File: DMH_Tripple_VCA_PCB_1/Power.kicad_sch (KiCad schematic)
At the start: 14 parts, among them J0 Conn_01x01, J100 IDC_02x05, J101 IDC_02x08

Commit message: Schematic in progress
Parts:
- removed C5: 47uF, Capacitor_THT:CP_Radial_D4.0mm_P1.50mm, symbol Device:C_Polarized
- removed C6: 100nF, Capacitor_THT:C_Disc_D4.3mm_W1.9mm_P5.00mm, symbol Device:C
- removed D3, D5: SB140+, Diode_THT:D_DO-41_SOD81_P10.16mm_Horizontal, symbol SynthStuff:Power_Bus_Schotty_+
- removed D4: SB140-, Diode_THT:D_DO-41_SOD81_P10.16mm_Horizontal, symbol SynthStuff:Power_Bus_Schotty_-
- removed J101: IDC_02x08, SynthStuff:IDC-Header_2x08_P2.54mm_Vertical_Eurorack, symbol SynthStuff:Eurorack_Power_Connector_16Pin
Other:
- note removed: "Delete what's not needed!"

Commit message: Finished Schematic
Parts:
- added C5, C6, C7, C8: 100nF, Capacitor_THT:C_Disc_D4.3mm_W1.9mm_P5.00mm, symbol Device:C
- added U1, U2: TL074, symbol Amplifier_Operational:TL074
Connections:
- net +12V: now also C5.1, C7.1, U1.4 (V+), U2.4 (V+)
- net -12V: now also C6.2, C8.2, U1.11 (V-), U2.11 (V-)
- net GND: now also C5.2, C6.1, C7.2, C8.1

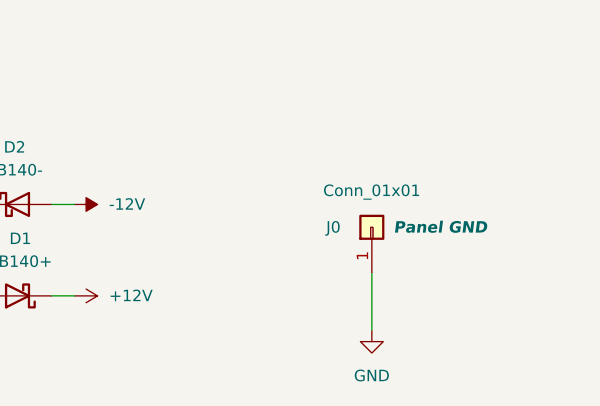
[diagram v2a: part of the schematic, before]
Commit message: PCB 1 component positioning in progress
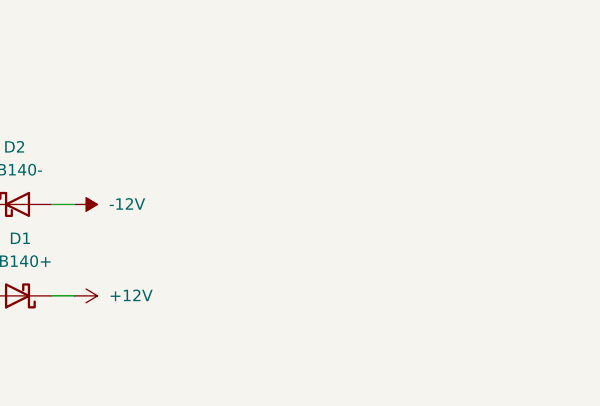
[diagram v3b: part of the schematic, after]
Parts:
- removed J0: Conn_01x01, Connector_PinHeader_2.54mm:PinHeader_1x01_P2.54mm_Vertical, symbol Connector_Generic:Conn_01x01
- U1, U2: footprint (none) -> Package_DIP:DIP-14_W7.62mm_Socket
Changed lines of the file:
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@@
-	(wire
-		(pts
-			(xy 152.4 182.88) (xy 152.4 189.23)
-		)
-		(stroke
-			(width 0)
-			(type default)
-		)
-	)
 	(wire
 		(pts
@@
 			)
 		)
-		(property "Footprint" ""
+		(property "Footprint" "Package_DIP:DIP-14_W7.62mm_Socket"
 			(at 52.07 118.11 0)
 			(effects
@@
 				)
 				(hide yes)
+			)
+		)
+		(property "Function" ""
+			(at 53.34 120.65 0)
+			(effects
+				(font
+					(size 1.27 1.27)
+				)
 			)
 		)
@@
 	)
 	(symbol
-		(lib_id "Connector_Generic:Conn_01x01")
-		(at 152.4 177.8 90)
-		(unit 1)
-		(exclude_from_sim no)
-		(in_bom yes)
-		(on_board yes)
-		(dnp no)
-		(property "Reference" "J0"
-			(at 147.32 177.8 90)
-			(effects
-				(font
-					(size 1.27 1.27)
-				)
-				(justify right)
-			)
-		)
-		(property "Value" "Conn_01x01"
-			(at 152.4 173.736 90)
-			(effects
-				(font
-					(size 1.27 1.27)
-				)
-			)
-		)
-		(property "Footprint" "Connector_PinHeader_2.54mm:PinHeader_1x01_P2.54mm_Vertical"
-			(at 152.4 177.8 0)
-			(effects
-				(font
-					(size 1.27 1.27)
-				)
-				(hide yes)
-			)
-		)
-		(property "Datasheet" "~"
-			(at 152.4 177.8 0)
-			(effects
-				(font
-					(size 1.27 1.27)
-				)
-				(hide yes)
-			)
-		)
-		(property "Description" "Generic connector, single row, 01x01, script generated (kicad-library-utils/schlib/autogen/connector/)"
-			(at 152.4 177.8 0)
-			(effects
-				(font
-					(size 1.27 1.27)
-				)
-				(hide yes)
-			)
-		)
-		(property "Function" "Panel GND"
-			(at 160.02 177.8 90)
-			(effects
-				(font
-					(size 1.27 1.27)
-					(thickness 0.254)
-					(bold yes)
-					(italic yes)
-				)
-			)
-		)
-		(pin "1"
-		)
-		(instances
-			(project "DMH-Kosmo-5cm-PCB"
-				(path "/58f4306d-5387-4983-bb08-41a2313fd315/0cdf34b2-39cd-4d9e-981a-97cd34791509"
-					(reference "J0")
-					(unit 1)
-				)
-			)
-		)
-	)
-	(symbol
 		(lib_id "power:+12V")
 		(at 17.78 95.25 0)
@@
 	)
 	(symbol
-		(lib_id "power:GND")
-		(at 152.4 189.23 0)
-		(unit 1)
-		(exclude_from_sim no)
-		(in_bom yes)
-		(on_board yes)
-		(dnp no)
-		(fields_autoplaced yes)
-		(property "Reference" "#PWR08"
-			(at 152.4 195.58 0)
-			(effects
-				(font
-					(size 1.27 1.27)
-				)
-				(hide yes)
-			)
-		)
-		(property "Value" "GND"
-			(at 152.4 194.31 0)
-			(effects
-				(font
-					(size 1.27 1.27)
-				)
-			)
-		)
-		(property "Footprint" ""
-			(at 152.4 189.23 0)
-			(effects
-				(font
-					(size 1.27 1.27)
-				)
-				(hide yes)
-			)
-		)
-		(property "Datasheet" ""
-			(at 152.4 189.23 0)
-			(effects
-				(font
-					(size 1.27 1.27)
-				)
-				(hide yes)
-			)
-		)
-		(property "Description" "Power symbol creates a global label with name \"GND\" , ground"
-			(at 152.4 189.23 0)
-			(effects
-				(font
-					(size 1.27 1.27)
-				)
-				(hide yes)
-			)
-		)
-		(pin "1"
-		)
-		(instances
-			(project "DMH-Kosmo-5cm-PCB"
-				(path "/58f4306d-5387-4983-bb08-41a2313fd315/0cdf34b2-39cd-4d9e-981a-97cd34791509"
-					(reference "#PWR08")
-					(unit 1)
-				)
-			)
-		)
-	)
-	(symbol
 		(lib_id "Device:C")
 		(at 38.1 133.35 0)
@@
 			)
 		)
-		(property "Footprint" ""
+		(property "Footprint" "Package_DIP:DIP-14_W7.62mm_Socket"
 			(at 77.47 118.11 0)
 			(effects
@@
 			)
 		)
+		(property "Function" ""
+			(at 78.74 120.65 0)
+			(effects
+				(font
+					(size 1.27 1.27)
+				)
+			)
+		)
